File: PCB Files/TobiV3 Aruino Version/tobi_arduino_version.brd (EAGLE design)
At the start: 103 x 74 mm, 45 parts

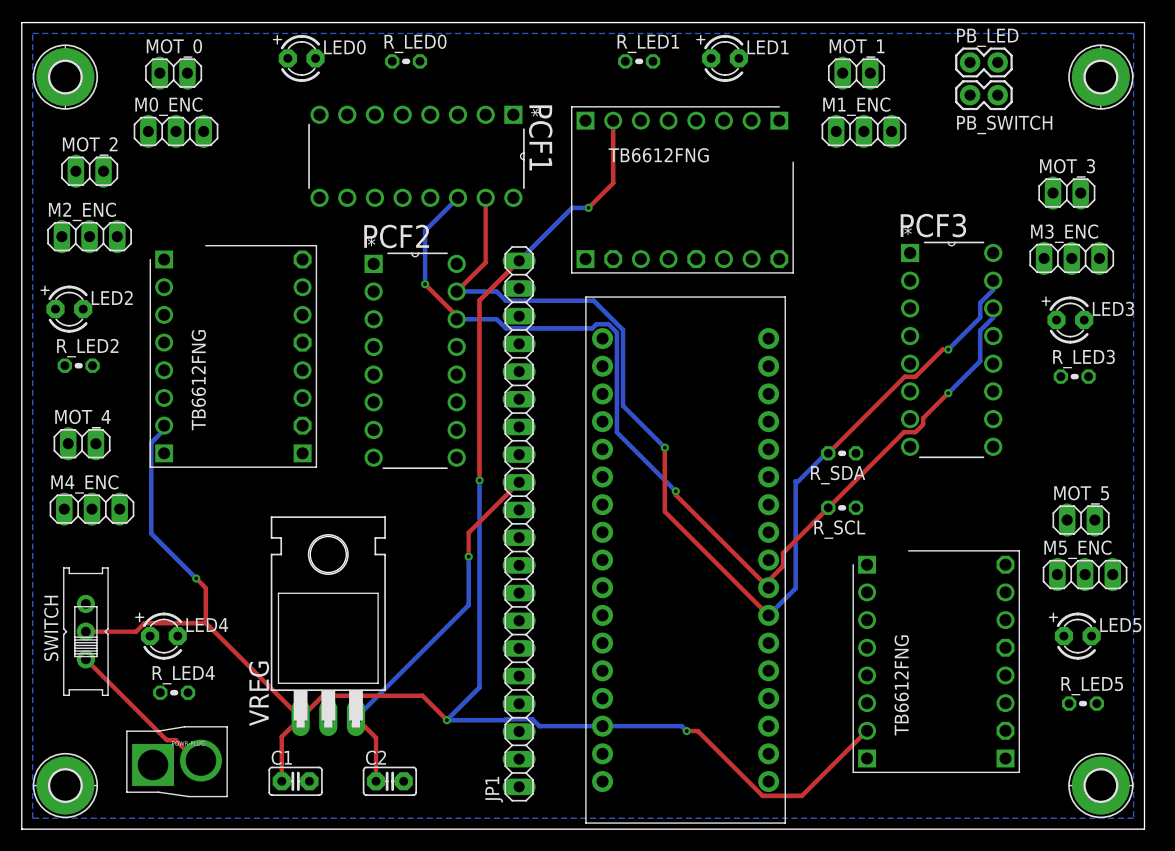
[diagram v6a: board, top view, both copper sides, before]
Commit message: route motor leads with heavy traces
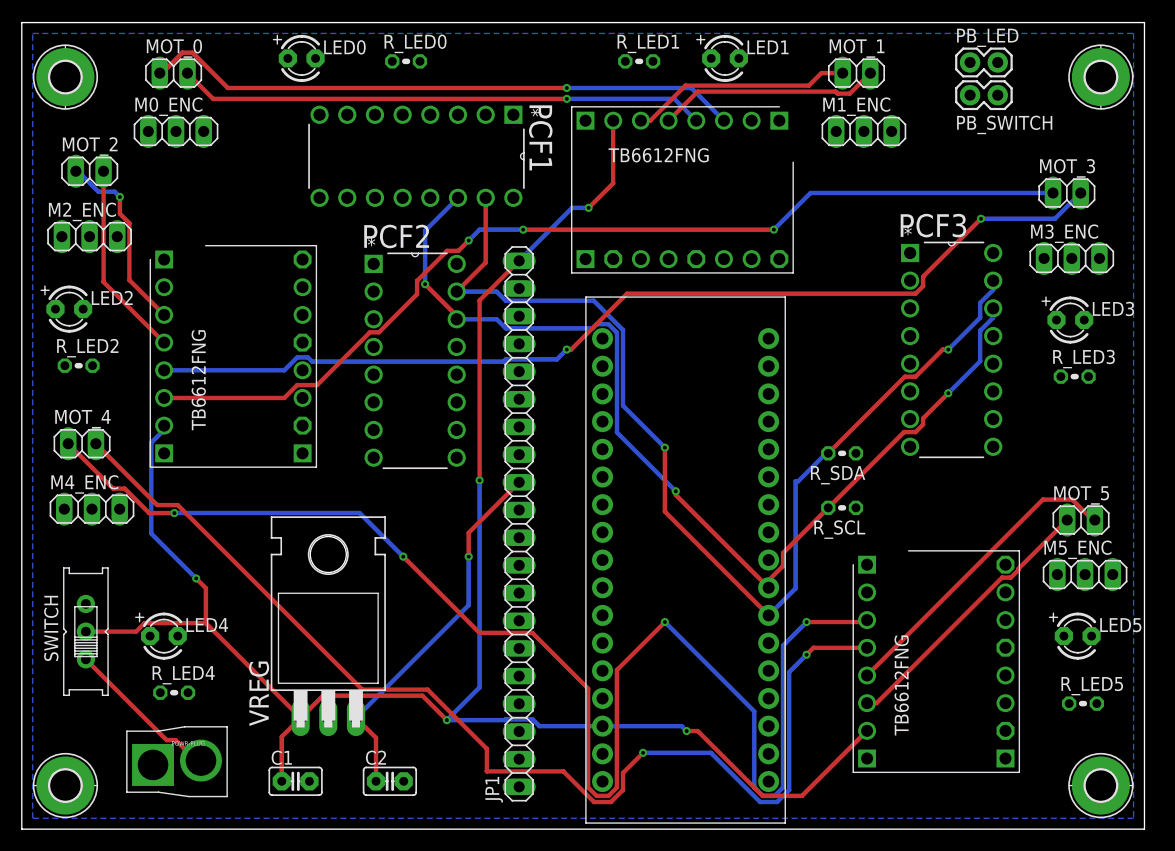
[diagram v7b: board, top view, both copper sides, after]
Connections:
- removed net M3_M4_EN: DRIVER2.STBY
- net M2_M3_EN: now also DRIVER2.STBY
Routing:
- net M4_A: track 0.00 -> 129.9 mm, vias 0 -> 4
- net M4_B: track 0.00 -> 102.4 mm, vias 0 -> 2
- net M3_B: track 0.00 -> 91.7 mm, vias 0 -> 2
- net M3_A: track 0.00 -> 90.1 mm, vias 0 -> 3
- net M0_A: track 0.00 -> 55.1 mm, vias 0 -> 1
- net M0_B: track 0.00 -> 48.5 mm, vias 0 -> 1
- net M5_B: track 0.00 -> 28.4 mm
- net M5_A: track 0.00 -> 25.4 mm
- net M1_B: track 0.00 -> 20.5 mm
- net M1_A: track 0.00 -> 20.3 mm
- net M2_B: track 0.00 -> 18.0 mm
- net M2_A: track 0.00 -> 17.5 mm, vias 0 -> 1

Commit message: autoroute the rest, i'm not happy with the vias near pcf1
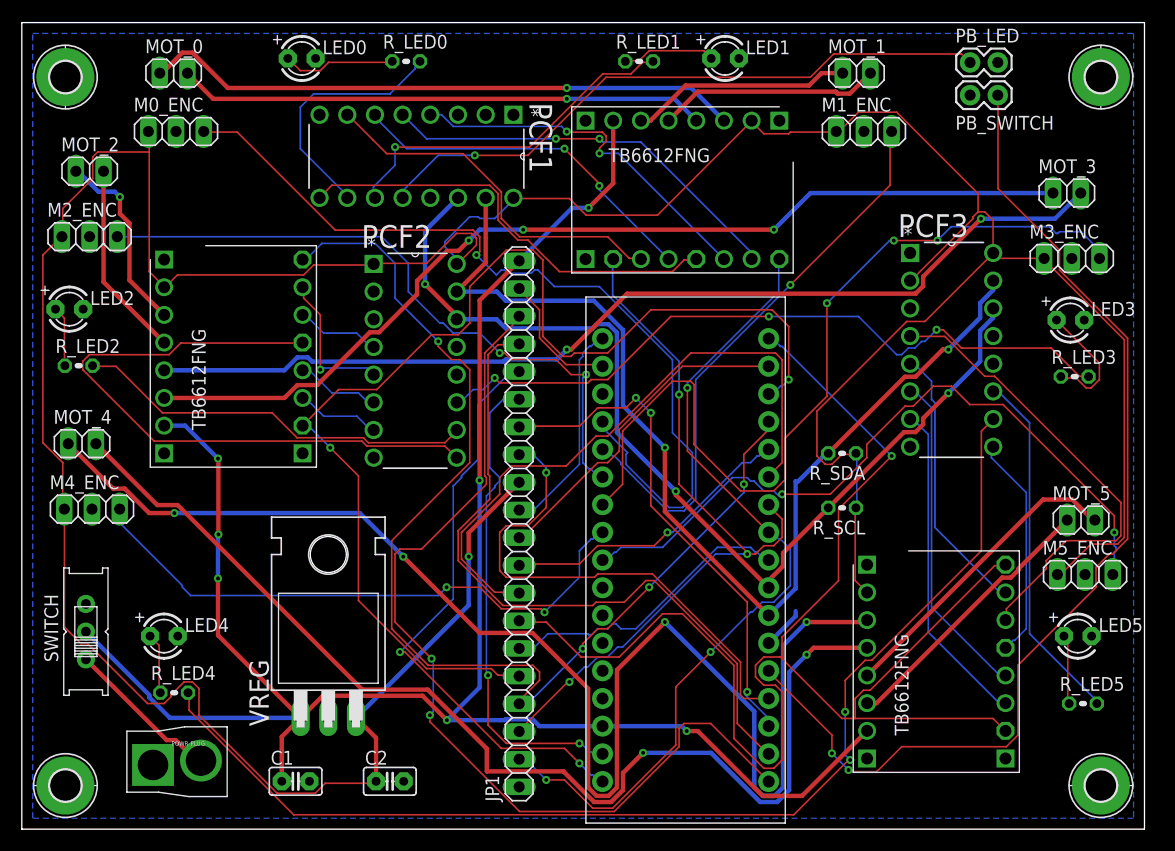
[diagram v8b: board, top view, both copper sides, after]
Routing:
- net VCC: track 34.4 -> 335.5 mm
- net M5_PWM: track 0.00 -> 132.9 mm, vias 0 -> 1
- net M3_PWM: track 0.00 -> 107.2 mm, vias 0 -> 2
- net LED4: track 0.00 -> 105.8 mm, vias 0 -> 2
- net M2_PWM: track 0.00 -> 104.9 mm, vias 0 -> 4
- net RESET: track 0.00 -> 97.1 mm, vias 0 -> 2
- net MOSI: track 0.00 -> 85.9 mm, vias 0 -> 2
- net M0_ENC: track 0.06 -> 80.2 mm, vias 0 -> 1
- net M3_ENC: track 0.00 -> 80.0 mm, vias 0 -> 3
- net M0_PWM: track 0.00 -> 76.0 mm, vias 0 -> 3
- net M1_PWM: track 0.00 -> 67.3 mm, vias 0 -> 3
- net M5_ENC: track 0.00 -> 66.2 mm, vias 0 -> 2
- net LED3: track 0.00 -> 65.8 mm, vias 0 -> 3
- net SS: track 0.00 -> 64.3 mm
- net M2_ENC: track 0.00 -> 60.3 mm, vias 0 -> 2
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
